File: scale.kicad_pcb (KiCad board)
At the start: 4 copper layers, 80 x 60 mm, 53 parts, among them J1 Conn_01x02_Pin, J2 Conn_01x04_Pin, J3 Conn_01x05_Pin, J4 Conn_01x05_Pin, Q1 S8050, Q2 S8050, Q3 MMBT3904, SW1 SW_Push, U1 HLK-10M12, U2 LM2576HVS-5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

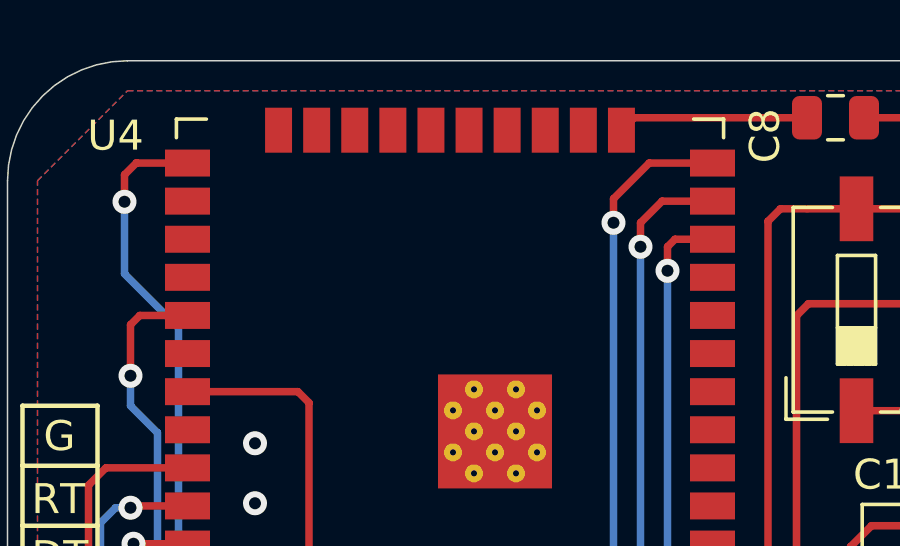
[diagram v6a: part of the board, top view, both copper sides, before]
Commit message: change DATA, BZR, and DOT pins
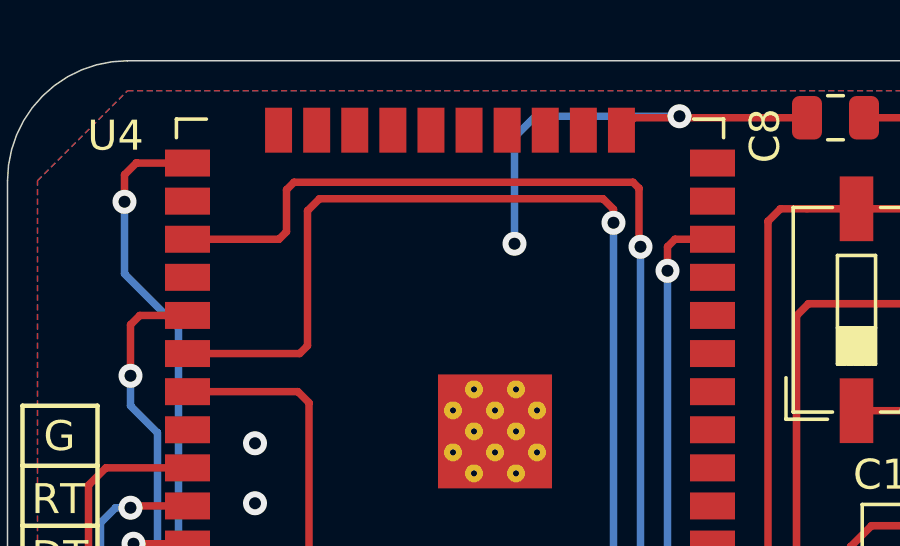
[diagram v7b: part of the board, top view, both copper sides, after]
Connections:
- U4 pad 13: /display/DATA -> unconnected-(U4-IO14-Pad13)
- U4 pad 14: /display/DOT -> unconnected-(U4-IO12-Pad14)
- U4 pad 27: unconnected-(U4-IO16-Pad27) -> /display/DATA
- U4 pad 30: unconnected-(U4-IO18-Pad30) -> /display/DOT
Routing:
- net /display/DATA: track 58.3 -> 73.5 mm
- net /display/DOT: track 58.5 -> 73.5 mm
- net GND: track 153.0 -> 162.3 mm, vias 12 -> 14
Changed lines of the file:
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@@
   (net 48 "unconnected-(U4-IO15-Pad23)")
   (net 49 "unconnected-(U4-IO4-Pad26)")
-  (net 50 "unconnected-(U4-IO16-Pad27)")
+  (net 50 "unconnected-(U4-IO14-Pad13)")
   (net 51 "unconnected-(U4-IO17-Pad28)")
   (net 52 "Net-(BZ1-+)")
-  (net 53 "unconnected-(U4-IO18-Pad30)")
+  (net 53 "unconnected-(U4-IO12-Pad14)")
   (net 54 "unconnected-(U4-IO2-Pad24)")
   (net 55 "unconnected-(U4-NC-Pad32)")
@@
       (net 41 "/display/CLOCK") (pinfunction "IO27") (pintype "bidirectional"))
     (pad "13" smd rect (at -8.75 6.985 180) (size 1.5 0.9) (layers "F.Cu" "F.Paste" "F.Mask")
-      (net 40 "/display/DATA") (pinfunction "IO14") (pintype "bidirectional"))
+      (net 50 "unconnected-(U4-IO14-Pad13)") (pinfunction "IO14") (pintype "bidirectional"))
     (pad "14" smd rect (at -8.75 8.255 180) (size 1.5 0.9) (layers "F.Cu" "F.Paste" "F.Mask")
-      (net 39 "/display/DOT") (pinfunction "IO12") (pintype "bidirectional"))
+      (net 53 "unconnected-(U4-IO12-Pad14)") (pinfunction "IO12") (pintype "bidirectional"))
     (pad "15" smd rect (at -5.715 9.35 270) (size 1.5 0.9) (layers "F.Cu" "F.Paste" "F.Mask")
       (net 2 "GND") (pinfunction "GND") (pintype "passive"))
@@
       (net 49 "unconnected-(U4-IO4-Pad26)") (pinfunction "IO4") (pintype "bidirectional"))
     (pad "27" smd rect (at 8.75 5.715 180) (size 1.5 0.9) (layers "F.Cu" "F.Paste" "F.Mask")
-      (net 50 "unconnected-(U4-IO16-Pad27)") (pinfunction "IO16") (pintype "bidirectional"))
+      (net 40 "/display/DATA") (pinfunction "IO16") (pintype "bidirectional"))
     (pad "28" smd rect (at 8.75 4.445 180) (size 1.5 0.9) (layers "F.Cu" "F.Paste" "F.Mask")
       (net 51 "unconnected-(U4-IO17-Pad28)") (pinfunction "IO17") (pintype "bidirectional"))
@@
       (net 67 "/BUZZ") (pinfunction "IO5") (pintype "bidirectional"))
     (pad "30" smd rect (at 8.75 1.905 180) (size 1.5 0.9) (layers "F.Cu" "F.Paste" "F.Mask")
-      (net 53 "unconnected-(U4-IO18-Pad30)") (pinfunction "IO18") (pintype "bidirectional"))
+      (net 39 "/display/DOT") (pinfunction "IO18") (pintype "bidirectional"))
     (pad "31" smd rect (at 8.75 0.635 180) (size 1.5 0.9) (layers "F.Cu" "F.Paste" "F.Mask")
       (net 27 "/RDY_MCU") (pinfunction "IO19") (pintype "bidirectional"))
@@
   (via (at 33.6 9.6) (size 0.8) (drill 0.4) (layers "F.Cu" "B.Cu") (net 2))
   (via (at 14.45 38.05) (size 0.8) (drill 0.4) (layers "F.Cu" "B.Cu") (net 2))
+  (via (at 22.4 1.85) (size 0.8) (drill 0.4) (layers "F.Cu" "B.Cu") (net 2))
   (via (at 47.2 45.65) (size 0.8) (drill 0.4) (layers "F.Cu" "B.Cu") (net 2))
   (via (at 8.25 12.75) (size 0.8) (drill 0.4) (layers "F.Cu" "B.Cu") (net 2))
+  (via (at 16.9 6.1) (size 0.8) (drill 0.4) (layers "F.Cu" "B.Cu") (net 2))
   (via (at 56.5 51.5) (size 0.8) (drill 0.4) (layers "F.Cu" "B.Cu") (net 2))
   (via (at 8.25 14.75) (size 0.8) (drill 0.4) (layers "F.Cu" "B.Cu") (net 2))
   (segment (start 14.45 43.15) (end 14.45 38.05) (width 0.25) (layer "B.Cu") (net 2))
+  (segment (start 16.9 6.1) (end 16.9 2.55) (width 0.25) (layer "B.Cu") (net 2))
+  (segment (start 17.6 1.85) (end 22.4 1.85) (width 0.25) (layer "B.Cu") (net 2))
   (segment (start 1.9 22.1) (end 1.9 24.26) (width 0.25) (layer "B.Cu") (net 2))
   (segment (start 13.25 44.35) (end 14.45 43.15) (width 0.25) (layer "B.Cu") (net 2))
   (segment (start 51.8 18.9) (end 48 18.9) (width 0.6096) (layer "B.Cu") (net 2))
+  (segment (start 16.9 2.55) (end 17.6 1.85) (width 0.25) (layer "B.Cu") (net 2))
   (segment (start 52.200002 4.116604) (end 52.200002 18.499998) (width 0.6096) (layer "B.Cu") (net 2))
   (segment (start 52.200002 18.499998) (end 51.8 18.9) (width 0.6096) (layer "B.Cu") (net 2))
@@
   (segment (start 71.4384 52.704901) (end 71.4384 47.2384) (width 1.016) (layer "F.Cu") (net 29))
   (segment (start 23.2 46.2) (end 23.7 46.7) (width 0.25) (layer "F.Cu") (net 39))
-  (segment (start 23.5 3.41) (end 21.39 3.41) (width 0.25) (layer "F.Cu") (net 39))
+  (segment (start 10 9.5) (end 9.74 9.76) (width 0.25) (layer "F.Cu") (net 39))
   (segment (start 29.4 47.1) (end 29.4 47.3) (width 0.25) (layer "F.Cu") (net 39))
   (segment (start 23.7 46.7) (end 29 46.7) (width 0.25) (layer "F.Cu") (net 39))
-  (segment (start 21.39 3.41) (end 20.2 4.6) (width 0.25) (layer "F.Cu") (net 39))
   (segment (start 29 46.7) (end 29.4 47.1) (width 0.25) (layer "F.Cu") (net 39))
   (segment (start 23.230876 36.746597) (end 23.2 36.715721) (width 0.25) (layer "F.Cu") (net 39))
+  (segment (start 10 5) (end 10 9.5) (width 0.25) (layer "F.Cu") (net 39))
   (segment (start 29.4 51.3125) (end 29.4 47.3) (width 0.25) (layer "F.Cu") (net 39))
-  (segment (start 20.2 4.6) (end 20.2 5.4) (width 0.25) (layer "F.Cu") (net 39))
+  (segment (start 20.2 5.4) (end 20.2 4.95) (width 0.25) (layer "F.Cu") (net 39))
+  (segment (start 10.4 4.6) (end 10 5) (width 0.25) (layer "F.Cu") (net 39))
+  (segment (start 20.2 4.95) (end 19.85 4.6) (width 0.25) (layer "F.Cu") (net 39))
   (segment (start 23.2 36.715721) (end 23.2 46.2) (width 0.25) (layer "F.Cu") (net 39))
+  (segment (start 9.74 9.76) (end 6 9.76) (width 0.25) (layer "F.Cu") (net 39))
+  (segment (start 19.85 4.6) (end 10.4 4.6) (width 0.25) (layer "F.Cu") (net 39))
   (via (at 20.2 5.4) (size 0.8) (drill 0.4) (layers "F.Cu" "B.Cu") (net 39))
   (via (at 23.2 36.5) (size 0.8) (drill 0.4) (layers "F.Cu" "B.Cu") (net 39))
@@
   (segment (start 23.2 21.1) (end 23.2 21.3) (width 0.25) (layer "B.Cu") (net 39))
   (segment (start 20.2 20.2) (end 20.6 20.6) (width 0.25) (layer "B.Cu") (net 39))
-  (segment (start 23.5 4.68) (end 21.82 4.68) (width 0.25) (layer "F.Cu") (net 40))
-  (segment (start 21.1 5.4) (end 21.1 6.2) (width 0.25) (layer "F.Cu") (net 40))
+  (segment (start 6 5.95) (end 9.05 5.95) (width 0.25) (layer "F.Cu") (net 40))
   (segment (start 29.9 45.7) (end 24.65 45.7) (width 0.25) (layer "F.Cu") (net 40))
   (segment (start 24.5 45.7) (end 24.65 45.7) (width 0.25) (layer "F.Cu") (net 40))
   (segment (start 30.2 48.8) (end 30.2 46) (width 0.25) (layer "F.Cu") (net 40))
+  (segment (start 9.3 4.3) (end 9.55 4.05) (width 0.25) (layer "F.Cu") (net 40))
+  (segment (start 9.3 5.7) (end 9.3 4.3) (width 0.25) (layer "F.Cu") (net 40))
   (segment (start 31.9 51.3125) (end 31.9 49.5) (width 0.25) (layer "F.Cu") (net 40))
   (segment (start 30.5 49.1) (end 30.2 48.8) (width 0.25) (layer "F.Cu") (net 40))
@@
   (segment (start 31.9 49.5) (end 31.5 49.1) (width 0.25) (layer "F.Cu") (net 40))
   (segment (start 24.2 45.4) (end 24.5 45.7) (width 0.25) (layer "F.Cu") (net 40))
+  (segment (start 21.05 6.15) (end 21.1 6.2) (width 0.25) (layer "F.Cu") (net 40))
   (segment (start 24.2 36.500003) (end 24.2 45.4) (width 0.25) (layer "F.Cu") (net 40))
+  (segment (start 9.55 4.05) (end 20.85 4.05) (width 0.25) (layer "F.Cu") (net 40))
   (segment (start 24.199997 36.5) (end 24.2 36.500003) (width 0.25) (layer "F.Cu") (net 40))
-  (segment (start 21.82 4.68) (end 21.1 5.4) (width 0.25) (layer "F.Cu") (net 40))
+  (segment (start 21.05 4.25) (end 21.05 6.15) (width 0.25) (layer "F.Cu") (net 40))
+  (segment (start 9.05 5.95) (end 9.3 5.7) (width 0.25) (layer "F.Cu") (net 40))
+  (segment (start 20.85 4.05) (end 21.05 4.25) (width 0.25) (layer "F.Cu") (net 40))
   (via (at 21.1 6.2) (size 0.8) (drill 0.4) (layers "F.Cu" "B.Cu") (net 40))
   (via (at 24.2 36.5) (size 0.8) (drill 0.4) (layers "F.Cu" "B.Cu") (net 40))
